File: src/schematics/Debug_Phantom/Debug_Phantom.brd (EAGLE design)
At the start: 160 x 100 mm, 2 parts

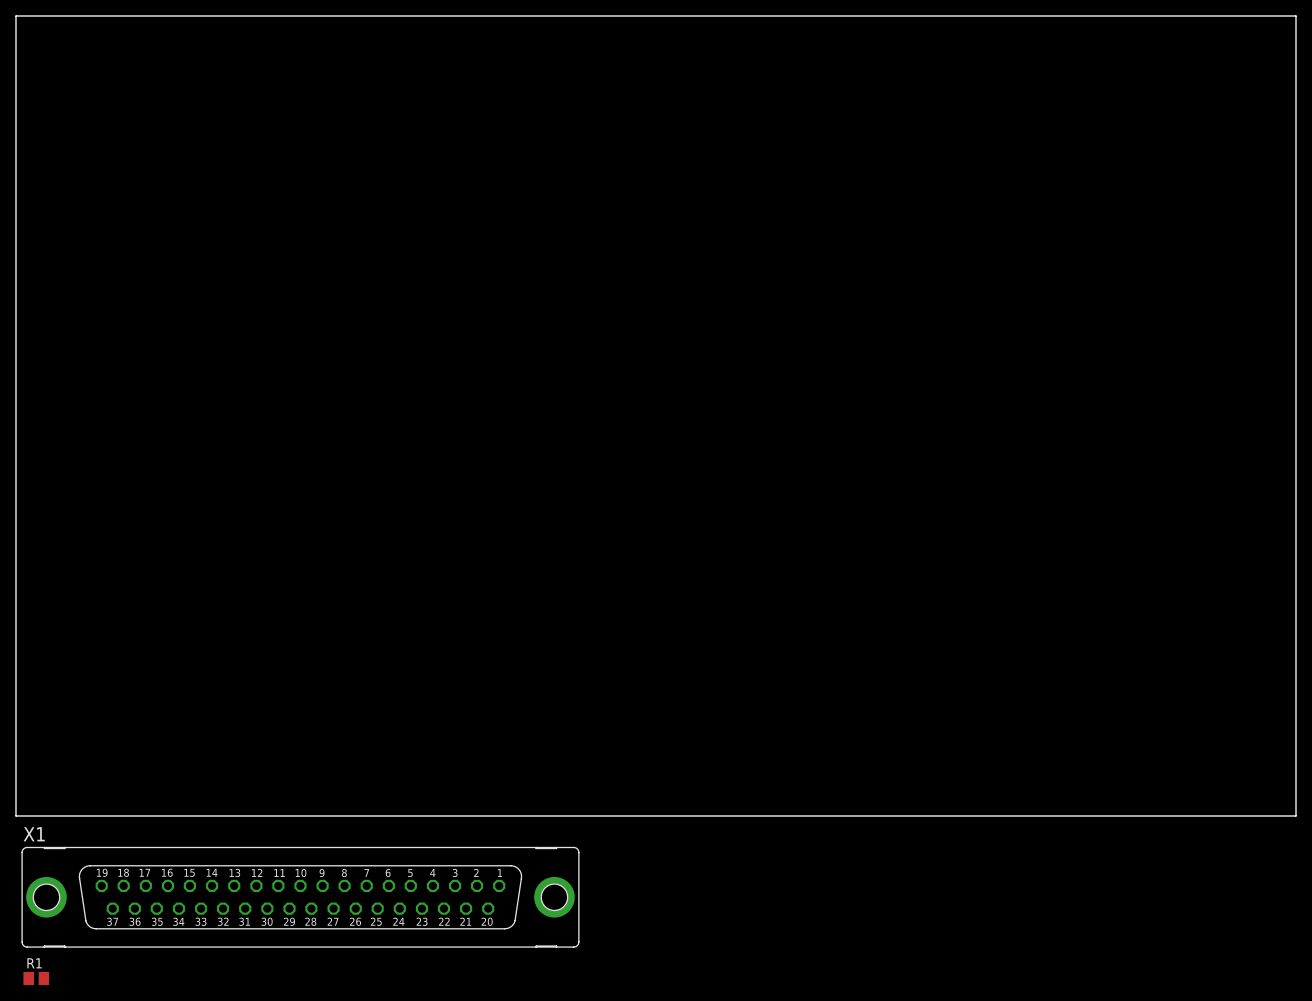
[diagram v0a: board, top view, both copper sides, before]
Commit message: debug phantom before routing
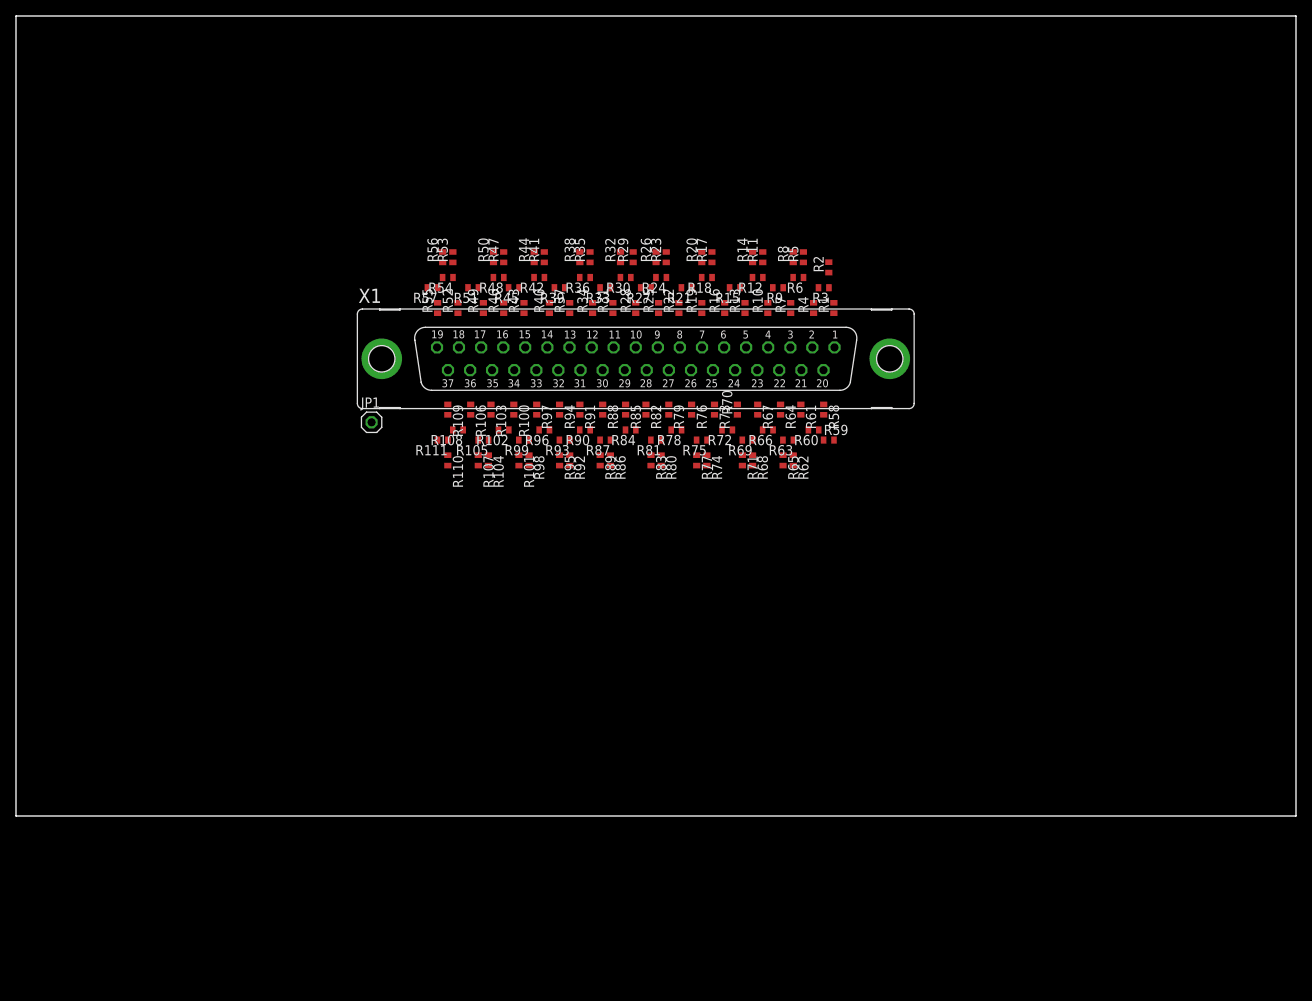
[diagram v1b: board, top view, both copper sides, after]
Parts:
- added JP1: (no value), pinhead:1X01
- added R10, R100, R101, R102, R103, R104, R105, R106, R107, R108, R109, R11, R110, R111, R12, R13, R14, R15, R16, R17, R18, R19, R2, R20, R21, R22, R23, R24, R25, R26, R27, R28, R29, R3, R30, R31, R32, R33, R34, R35, R36, R37, R38, R39, R4, R40, R41, R42, R43, R44, R45, R46, R47, R48, R49, R5, R50, R51, R52, R53, R54, R55, R56, R57, R58, R59, R6, R60, R61, R62, R63, R64, R65, R66, R67, R68, R69, R7, R70, R71, R72, R73, R74, R75, R76, R77, R78, R79, R8, R80, R81, R82, R83, R84, R85, R86, R87, R88, R89, R9, R90, R91, R92, R93, R94, R95, R96, R97, R98, R99: (no value), rcl:R0402
- R1: device rcl:M0805 -> rcl:R0402
- moved R1 130.2 mm to (102.2, 63.5), turned to 90 degrees
- moved X1 79.3 mm to (77.5, 57.1)
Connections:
- new net E1: R1.1, X1.1
- new net E10: R28.1, X1.10
- new net E11: R31.1, X1.11
- new net E12: R34.1, X1.12
- new net E13: R37.1, X1.13
- new net E14: R40.1, X1.14
- new net E15: R43.1, X1.15
- new net E16: R46.1, X1.16
- new net E17: R49.1, X1.17
- new net E18: R52.1, X1.18
- new net E19: R55.1, X1.19
- new net E2: R4.1, X1.2
- new net E20: R58.1, X1.20
- new net E21: R61.1, X1.21
- new net E22: R64.1, X1.22
- new net E23: R67.1, X1.23
- new net E24: R70.1, X1.24
- new net E25: R73.1, X1.25
- new net E26: R76.1, X1.26
- new net E27: R79.1, X1.27
- new net E28: R82.1, X1.28
- new net E29: R85.1, X1.29
- new net E3: R7.1, X1.3
- new net E30: R88.1, X1.30
- new net E31: R91.1, X1.31
- new net E32: R94.1, X1.32
- new net E33: R97.1, X1.33
- new net E34: R100.1, X1.34
- new net E35: R103.1, X1.35
- new net E36: R106.1, X1.36
- new net E37: R109.1, X1.37
- new net E38: R1.2, R111.2, R2.1, R3.1
- new net E39: R3.2, R4.2, R5.1, R6.1
- new net E4: R10.1, X1.4
- new net E40: R6.2, R7.2, R8.1, R9.1
- new net E41: R10.2, R11.1, R12.1, R9.2
- new net E42: R12.2, R13.2, R14.1, R15.1
- new net E43: R15.2, R16.2, R17.1, R18.1
- new net E44: R18.2, R19.2, R20.1, R21.1
- new net E45: R21.2, R22.2, R23.1, R24.1
- new net E46: R24.2, R25.2, R26.1, R27.1
- new net E47: R27.2, R28.2, R29.1, R30.1
- new net E48: R30.2, R31.2, R32.1, R33.1
- new net E49: R33.2, R34.2, R35.1, R36.1
- new net E5: R13.1, X1.5
- new net E50: R36.2, R37.2, R38.1, R39.1
- new net E51: R39.2, R40.2, R41.1, R42.1
- new net E52: R42.2, R43.2, R44.1, R45.1
- new net E53: R45.2, R46.2, R47.1, R48.1
- new net E54: R48.2, R49.2, R50.1, R51.1
- new net E55: R51.2, R52.2, R53.1, R54.1
- new net E56: R54.2, R55.2, R56.1, R57.1
- new net E57: R57.2, R58.2, R59.1, R60.1
- new net E58: R60.2, R61.2, R62.1, R63.1
- new net E59: R63.2, R64.2, R65.1, R66.1
- new net E6: R16.1, X1.6
- new net E60: R66.2, R67.2, R68.1, R69.1
- new net E61: R69.2, R70.2, R71.1, R72.1
- new net E63: R75.2, R76.2, R77.1, R78.1
- new net E64: R78.2, R79.2, R80.1, R81.1
- new net E65: R81.2, R82.2, R83.1, R84.1
- new net E66: R84.2, R85.2, R86.1, R87.1
- new net E67: R87.2, R88.2, R89.1, R90.1
- new net E68: R90.2, R91.2, R92.1, R93.1
- new net E69: R93.2, R94.2, R95.1, R96.1
- new net E7: R19.1, X1.7
- new net E70: R96.2, R97.2, R98.1, R99.1
- new net E72: R102.2, R103.2, R104.1, R105.1
- new net E73: R105.2, R106.2, R107.1, R108.1
- new net E74: R108.2, R109.2, R110.1, R111.1
- new net E8: R22.1, X1.8
- new net E9: R25.1, X1.9
- new net GND: JP1.1, R101.2, R104.2, R107.2, R11.2, R110.2, R14.2, R17.2, R2.2, R20.2, R23.2, R26.2, R29.2, R32.2, R35.2, R38.2, R41.2, R44.2, R47.2, R5.2, R50.2, R53.2, R56.2, R59.2, R62.2, R65.2, R68.2, R71.2, R74.2, R77.2, R8.2, R80.2, R83.2, R86.2, R89.2, R92.2, R95.2, R98.2
- new net N$1: R72.2, R73.2, R74.1, R75.1
- new net N$2: R100.2, R101.1, R102.1, R99.2

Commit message: Finished Debug Phantom and made gerber files sent to PCBTrain
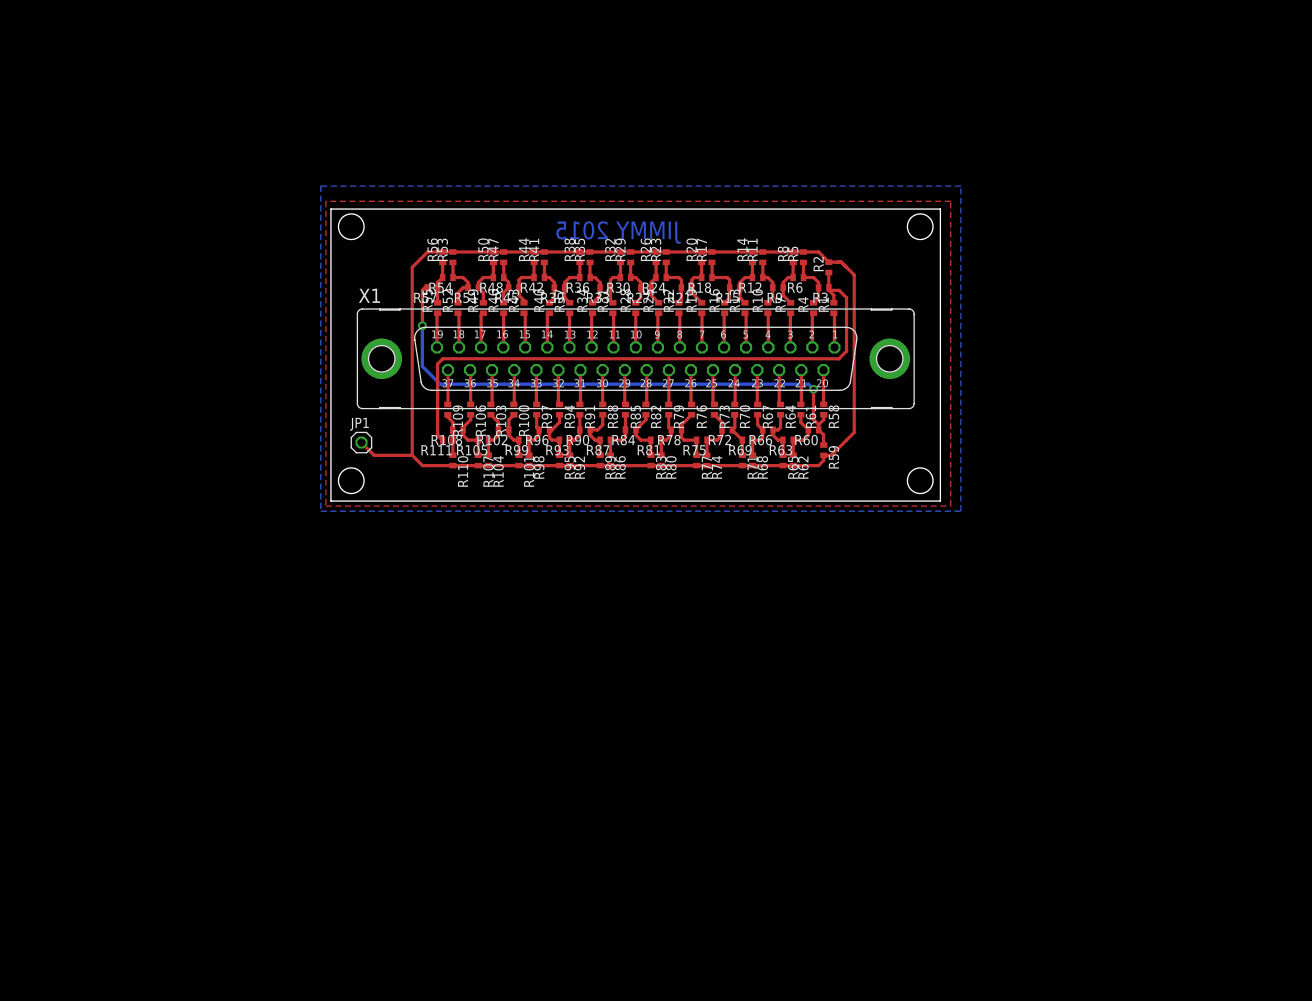
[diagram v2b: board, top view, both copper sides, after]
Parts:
- JP1: value (none) -> GNDHDR
- R1, R10, R100, R101, R102, R103, R104, R105, R106, R107, R108, R109, R11, R110, R111, R12, R13, R14, R15, R16, R17, R18, R19, R2, R20, R21, R22, R23, R24, R25, R26, R27, R28, R29, R3, R30, R31, R32, R33, R34, R35, R36, R37, R38, R39, R4, R40, R41, R42, R43, R44, R45, R46, R47, R48, R49, R5, R50, R51, R52, R53, R54, R55, R56, R57, R58, R59, R6, R60, R61, R62, R63, R64, R65, R66, R67, R68, R69, R7, R70, R71, R72, R73, R74, R75, R76, R77, R78, R79, R8, R80, R81, R82, R83, R84, R85, R86, R87, R88, R89, R9, R90, R91, R92, R93, R94, R95, R96, R97, R98, R99: value (none) -> 1k
- X1: value (none) -> DSUBIN
- moved JP1 2.84 mm to (43.2, 46.7)
- moved R59 1.42 mm to (101.0, 45.7), turned to 270 degrees
- moved R110 0.63 mm to (54.6, 44.5)
- moved R111 0.63 mm to (54.0, 47.0)
- moved R29 0.32 mm to (76.8, 69.8)
- moved R70 0.32 mm to (89.9, 50.8), turned to 270 degrees
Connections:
- net GND: now also X1.G1, X1.G2
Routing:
- net GND: track 0.00 -> 166.8 mm
- net E38: track 0.00 -> 74.9 mm
- net E57: track 0.00 -> 69.3 mm, vias 0 -> 2
- net E55: track 0.00 -> 7.47 mm
- net E43: track 0.00 -> 7.35 mm
- net E63: track 0.00 -> 7.30 mm
- net E67: track 0.00 -> 7.15 mm
- net E65: track 0.00 -> 7.10 mm
- net E52: track 0.00 -> 7.03 mm
- net N$1: track 0.00 -> 6.98 mm
- net E58: track 0.00 -> 6.97 mm
- net E73: track 0.00 -> 6.96 mm
- net E45: track 0.00 -> 6.89 mm
- net E39: track 0.00 -> 6.85 mm
- net E54: track 0.00 -> 6.83 mm
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- added copper zone on layer 1, net GND
- added copper zone on layer 16, net GND
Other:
- board size 160 x 100 mm -> 76.2 x 36.5 mm
- board text added: "DEBUG PHANTOM"
- board text added: "Gnd"
- board text added: "JIMMY 2015"
- board text added: "Please dont calibrate using this"
